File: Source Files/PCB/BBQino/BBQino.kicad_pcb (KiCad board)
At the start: 2 copper layers, 113 x 53.3 mm, 27 parts, among them J1 VIN < 13V, J2 230V input, J3 230V out, K1 FTR-MYAA005D, K2 FTR-MYAA005D, Q1 IPD068P03L3G, U1 ADP7142ARDZ-5.0, U99 24LC512

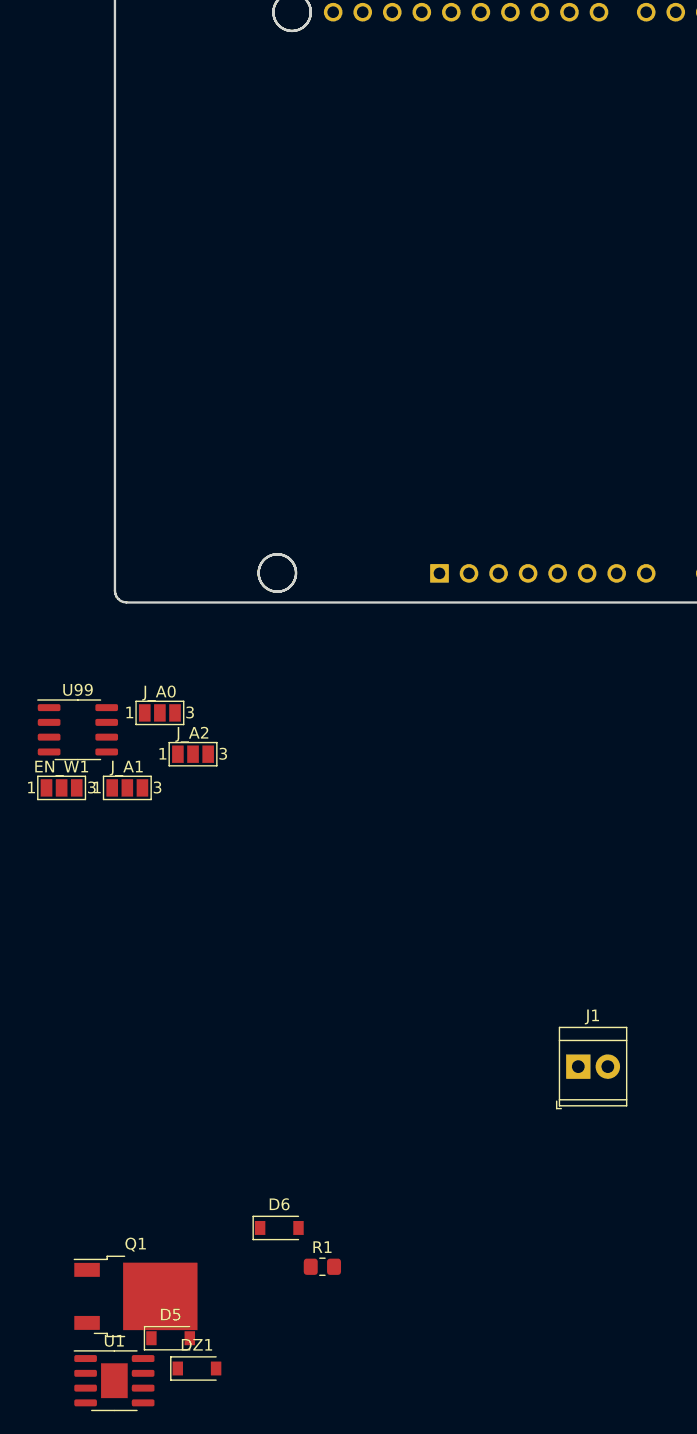
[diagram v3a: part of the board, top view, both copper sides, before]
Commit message: added thermocouple interface
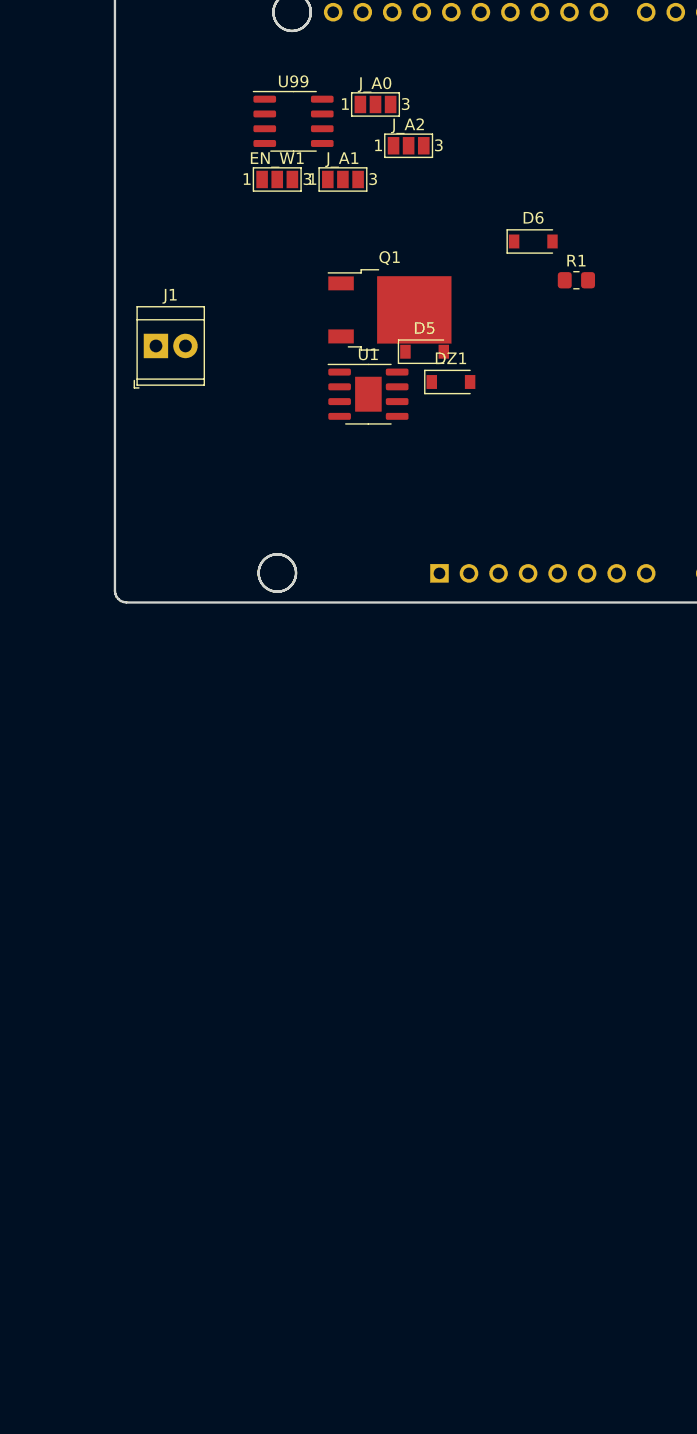
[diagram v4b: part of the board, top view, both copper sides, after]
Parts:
- moved D5 87.6 mm to (77.7, 60.9)
- moved DZ1 87.6 mm to (80.0, 63.6)
- moved R1 87.6 mm to (90.8, 54.8)
- moved D6 87.6 mm to (87.1, 51.5)
- moved Q1 87.6 mm to (74.7, 57.4)
- moved U1 87.6 mm to (72.9, 64.6)
- moved J1 71.8 mm to (54.6, 60.5)
- moved J_A0 55.5 mm to (73.5, 39.7)
- moved J_A2 55.5 mm to (76.3, 43.2)
- moved EN_W1 55.5 mm to (65.0, 46.1)
- moved J_A1 55.5 mm to (70.7, 46.1)
- moved U99 55.5 mm to (66.4, 41.1)
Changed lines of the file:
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@@
   )
   (module Diode_SMD:D_SOD-123 (layer F.Cu)
-    (at 65.221001 136.303001)
+    (at 87.065001 51.467001)
     (descr SOD-123)
     (tags SOD-123)
@@
   )
   (module Diode_SMD:D_SOD-123 (layer F.Cu)
-    (at 55.871001 145.783001)
+    (at 77.715001 60.947001)
     (descr SOD-123)
     (tags SOD-123)
@@
   )
   (module Package_SO:SOIC-8_3.9x4.9mm_P1.27mm (layer F.Cu)
-    (at 47.9 93.46)
+    (at 66.442 41.136)
     (descr "SOIC, 8 Pin (JEDEC MS-012AA, https://www.analog.com/media/en/package-pcb-resources/package/pkg_pdf/soic_narrow-r/r_8.pdf), generated with kicad-footprint-generator ipc_gullwing_generator.py")
     (tags "SOIC SO")
@@
   )
   (module Package_SO:SOIC-8-1EP_3.9x4.9mm_P1.27mm_EP2.29x3mm (layer F.Cu)
-    (at 51.036 149.438)
+    (at 72.88 64.602)
     (descr "SOIC, 8 Pin (https://www.analog.com/media/en/technical-documentation/data-sheets/ada4898-1_4898-2.pdf#page=29), generated with kicad-footprint-generator ipc_gullwing_generator.py")
     (tags "SOIC SO")
@@
   )
   (module Resistor_SMD:R_0805_2012Metric_Pad1.20x1.40mm_HandSolder (layer F.Cu)
-    (at 68.926 139.638)
+    (at 90.77 54.802)
     (descr "Resistor SMD 0805 (2012 Metric), square (rectangular) end terminal, IPC_7351 nominal with elongated pad for handsoldering. (Body size source: IPC-SM-782 page 72, https://www.pcb-3d.com/wordpress/wp-content/uploads/ipc-sm-782a_amendment_1_and_2.pdf), generated with kicad-footprint-generator")
     (tags "resistor handsolder")
@@
   )
   (module Package_TO_SOT_SMD:TO-252-2 (layer F.Cu)
-    (at 52.886 142.188)
+    (at 74.73 57.352)
     (descr "TO-252 / DPAK SMD package, http://www.infineon.com/cms/en/product/packages/PG-TO252/PG-TO252-3-1/")
     (tags "DPAK TO-252 DPAK-3 TO-252-3 SOT-428")
@@
   )
   (module Jumper:SolderJumper-3_P1.3mm_Open_Pad1.0x1.5mm_NumberLabels (layer F.Cu)
-    (at 57.8 95.56)
+    (at 76.342 43.236)
     (descr "SMD Solder Jumper, 1x1.5mm Pads, 0.3mm gap, open, labeled with numbers")
     (tags "solder jumper open")
@@
   )
   (module Jumper:SolderJumper-3_P1.3mm_Open_Pad1.0x1.5mm_NumberLabels (layer F.Cu)
-    (at 52.15 98.46)
+    (at 70.692 46.136)
     (descr "SMD Solder Jumper, 1x1.5mm Pads, 0.3mm gap, open, labeled with numbers")
     (tags "solder jumper open")
@@
   )
   (module Jumper:SolderJumper-3_P1.3mm_Open_Pad1.0x1.5mm_NumberLabels (layer F.Cu)
-    (at 54.95 92.01)
+    (at 73.492 39.686)
     (descr "SMD Solder Jumper, 1x1.5mm Pads, 0.3mm gap, open, labeled with numbers")
     (tags "solder jumper open")
@@
   )
   (module TerminalBlock_TE-Connectivity:TerminalBlock_TE_282834-2_1x02_P2.54mm_Horizontal (layer F.Cu)
-    (at 90.932 122.428)
+    (at 54.61 60.452)
     (descr "Terminal Block TE 282834-2, 2 pins, pitch 2.54mm, size 5.54x6.5mm^2, drill diamater 1.1mm, pad diameter 2.1mm, see http://www.te.com/commerce/DocumentDelivery/DDEController?Action=showdoc&DocId=Customer+Drawing%7F282834%7FC1%7Fpdf%7FEnglish%7FENG_CD_282834_C1.pdf, script-generated using https://github.com/pointhi/kicad-footprint-generator/scripts/TerminalBlock_TE-Connectivity")
     (tags "THT Terminal Block TE 282834-2 pitch 2.54mm size 5.54x6.5mm^2 drill 1.1mm pad 2.1mm")
@@
   )
   (module Jumper:SolderJumper-3_P1.3mm_Open_Pad1.0x1.5mm_NumberLabels (layer F.Cu)
-    (at 46.5 98.46)
+    (at 65.042 46.136)
     (descr "SMD Solder Jumper, 1x1.5mm Pads, 0.3mm gap, open, labeled with numbers")
     (tags "solder jumper open")
@@
   )
   (module Diode_SMD:D_SOD-123 (layer F.Cu)
-    (at 58.136 148.388)
+    (at 79.98 63.552)
     (descr SOD-123)
     (tags SOD-123)

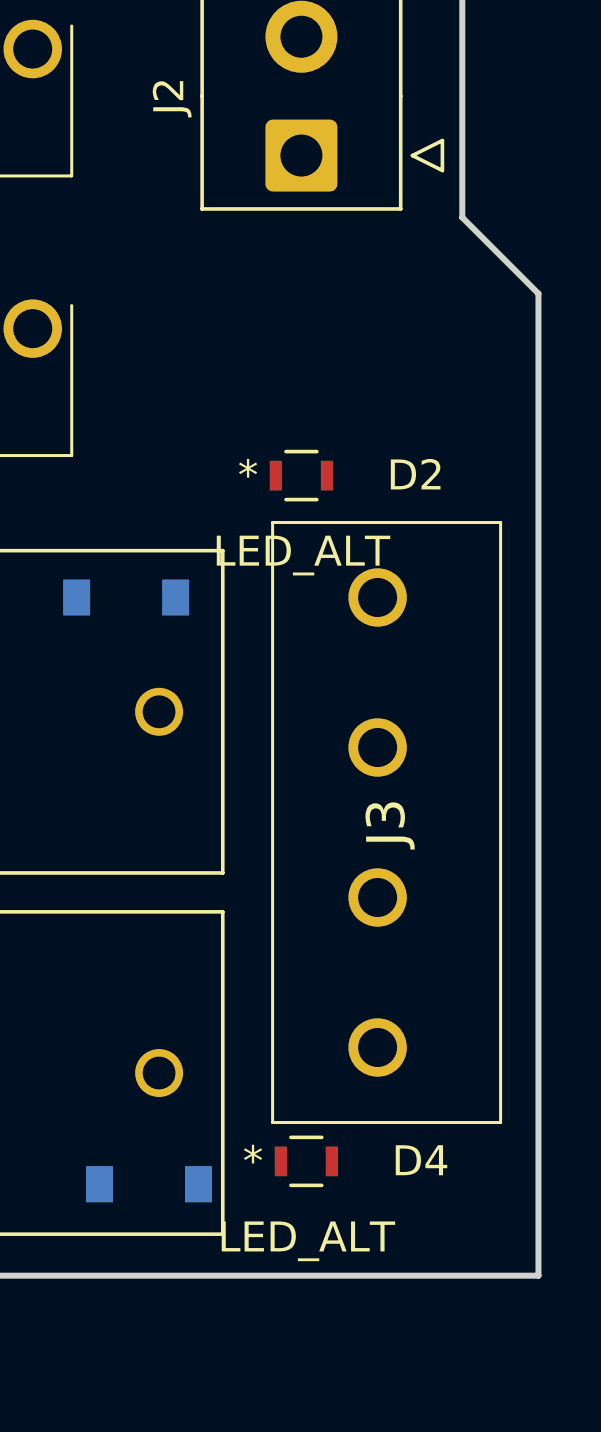
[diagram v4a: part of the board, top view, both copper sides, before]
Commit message: added current sense on motor side
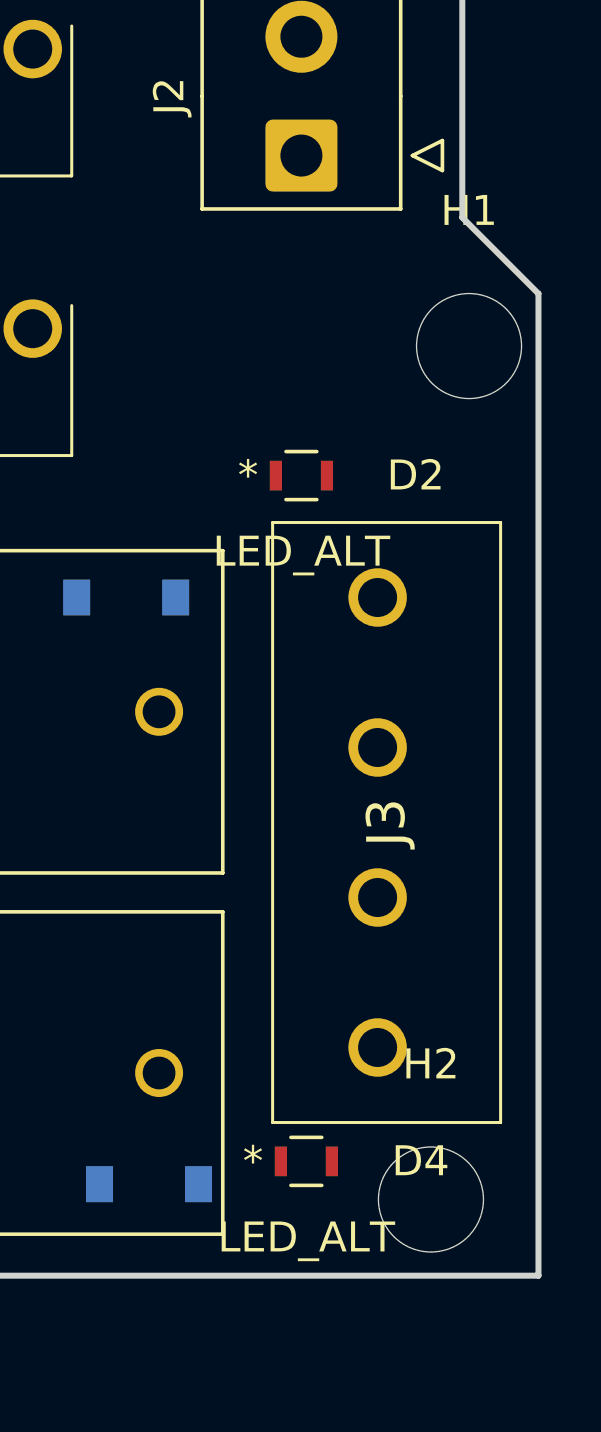
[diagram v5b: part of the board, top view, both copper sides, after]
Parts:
- added H1: MountingHole, MountingHole:MountingHole_3.5mm, F.Cu at (161.8, 46.2)
- added H2: MountingHole, MountingHole:MountingHole_3.5mm, F.Cu at (160.5, 74.7)

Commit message: updated schematic
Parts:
- added C2: 2.2uF, Capacitor_SMD:C_0805_2012Metric_Pad1.18x1.45mm_HandSolder, F.Cu at (55.9, 111.5)
- added C3: 10nF, Capacitor_SMD:C_0805_2012Metric_Pad1.18x1.45mm_HandSolder, F.Cu at (60.7, 111.5)
- added C4: 1nF, Capacitor_SMD:C_0805_2012Metric_Pad1.18x1.45mm_HandSolder, F.Cu at (80.2, 101.9)
- added C5: 2.2uF, Capacitor_SMD:C_0805_2012Metric_Pad1.18x1.45mm_HandSolder, F.Cu at (65.5, 111.5)
- added D7: 1N4148W-HF, Diode_SMD:D_SOD-123, F.Cu at (203.1, 66.8)
- added D8: 1N4148W-HF, Diode_SMD:D_SOD-123, F.Cu at (202.8, 61.6)
- added IC2: DG4052EEN-T1-GE4, BBQino:QFN40P180X260X60-16N-D, F.Cu at (104.2, 96.4)
- added IC3: MAX6675ISA+T, BBQino:SOIC127P600X175-8N, F.Cu at (97.9, 97.2)
- added K3: FINDER-40.41, Relay_THT:Relay_SPDT_Finder_40.41, F.Cu at (173.1, 51.6)
- added K4: FINDER-40.41, Relay_THT:Relay_SPDT_Finder_40.41, F.Cu at (173.1, 65.6)
- added Q2: DMP4051LK3, Package_TO_SOT_SMD:TO-252-3_TabPin2, F.Cu at (59.5, 97.9)
- added Q3: DMN4040SK3, Package_TO_SOT_SMD:TO-252-3_TabPin2, F.Cu at (59.5, 106.0)
- added Q4: DMP4051LK3, Package_TO_SOT_SMD:TO-252-3_TabPin2, F.Cu at (71.7, 97.9)
- added Q5: DMN4040SK3, Package_TO_SOT_SMD:TO-252-3_TabPin2, F.Cu at (71.7, 106.0)
- added Q6: 2N7002K, Package_TO_SOT_SMD:SOT-23, F.Cu at (203.1, 51.6)
- added Q7: 2N7002K, Package_TO_SOT_SMD:SOT-23, F.Cu at (207.6, 51.6)
- added R4: 330, Resistor_SMD:R_0805_2012Metric_Pad1.20x1.40mm_HandSolder, F.Cu at (70.3, 111.5)
- added R5: 330, Resistor_SMD:R_0805_2012Metric_Pad1.20x1.40mm_HandSolder, F.Cu at (80.2, 104.8)
- added U2: INA219AxD, Package_SO:SOIC-8_3.9x4.9mm_P1.27mm, F.Cu at (82.0, 97.1)
- added U3: INA181, Package_TO_SOT_SMD:SOT-23-6, F.Cu at (96.1, 106.4)
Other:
- board size 113 x 53.3 mm -> 158.5 x 53.3 mm

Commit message: New architecture
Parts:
- removed R4, R5: 330, Resistor_SMD:R_0805_2012Metric_Pad1.20x1.40mm_HandSolder
- removed U2: INA219AxD, Package_SO:SOIC-8_3.9x4.9mm_P1.27mm
- added C10: 1uF, Capacitor_SMD:C_0805_2012Metric_Pad1.18x1.45mm_HandSolder, F.Cu at (121.9, 10.6)
- added C11: 1uF, Capacitor_SMD:C_0805_2012Metric_Pad1.18x1.45mm_HandSolder, F.Cu at (113.9, 19.7)
- added C12: 1uF, Capacitor_SMD:C_0805_2012Metric_Pad1.18x1.45mm_HandSolder, F.Cu at (126.7, 7.62)
- added C19: 1uF, Capacitor_SMD:C_0805_2012Metric_Pad1.18x1.45mm_HandSolder, F.Cu at (118.7, 16.7)
- added C20: 1uF, Capacitor_SMD:C_0805_2012Metric_Pad1.18x1.45mm_HandSolder, F.Cu at (121.9, 13.6)
- added C21: 1uF, Capacitor_SMD:C_0805_2012Metric_Pad1.18x1.45mm_HandSolder, F.Cu at (126.7, 10.6)
- added C8: 2.2nF, Capacitor_SMD:C_0805_2012Metric_Pad1.18x1.45mm_HandSolder, F.Cu at (121.9, 7.62)
- added C9: 2.2nF, Capacitor_SMD:C_0805_2012Metric_Pad1.18x1.45mm_HandSolder, F.Cu at (113.9, 16.7)
- added D10: BAS316, Diode_SMD:D_SOD-323, F.Cu at (93.3, 49.1)
- added D11: BAS316, Diode_SMD:D_SOD-323, F.Cu at (74.6, 78.8)
- added D12: BAS316, Diode_SMD:D_SOD-323, F.Cu at (93.8, 45.4)
- added D13: BAS316, Diode_SMD:D_SOD-323, F.Cu at (89.1, 49.1)
- added D14: BAS316, Diode_SMD:D_SOD-323, F.Cu at (126.5, 13.6)
- added D15: BAS316, Diode_SMD:D_SOD-323, F.Cu at (118.4, 19.7)
- added D16: B140-E3, Diode_SMD:D_SMA, F.Cu at (115.5, 8.39)
- added D17: B140-E3, Diode_SMD:D_SMA, F.Cu at (115.5, 12.9)
- added D18: BZM55Bxx, Diode_SMD:D_MicroMELF, F.Cu at (131.8, 16.6)
- added D19: BZM55Bxx, Diode_SMD:D_MicroMELF, F.Cu at (131.8, 19.3)
- added D9: SD36_SOD323, Diode_SMD:D_SOD-323, F.Cu at (101.8, 36.5)
- added J4: 230V_1_presence, TerminalBlock_Phoenix:TerminalBlock_Phoenix_PT-1,5-2-3.5-H_1x02_P3.50mm_Horizontal, F.Cu at (134.6, 38.1)
- added J5: Screw_Terminal_01x02-Connector, TerminalBlock_Phoenix:TerminalBlock_Phoenix_PT-1,5-2-3.5-H_1x02_P3.50mm_Horizontal, F.Cu at (55.9, 61.0)
- added J6: 230v_2_presence, TerminalBlock_Phoenix:TerminalBlock_Phoenix_PT-1,5-2-3.5-H_1x02_P3.50mm_Horizontal, F.Cu at (142.2, 38.1)
- added Q10: IPD025N06N, Package_TO_SOT_SMD:TO-252-3_TabPin2, F.Cu at (101.5, 58.1)
- added Q11: IPD025N06N, Package_TO_SOT_SMD:TO-252-3_TabPin2, F.Cu at (101.5, 66.2)
- added Q12: BC846BPN, Package_TO_SOT_SMD:SOT-363_SC-70-6, F.Cu at (127.7, 17.1)
- added Q13: BC846BPN, Package_TO_SOT_SMD:SOT-363_SC-70-6, F.Cu at (135.7, 12.6)
- added Q8: IPD025N06N, Package_TO_SOT_SMD:TO-252-3_TabPin2, F.Cu at (89.4, 58.1)
- added Q9: IPD025N06N, Package_TO_SOT_SMD:TO-252-3_TabPin2, F.Cu at (89.4, 66.2)
- added R18: 10, Resistor_SMD:R_0805_2012Metric_Pad1.20x1.40mm_HandSolder, F.Cu at (90.4, 71.7)
- added R19: 10, Resistor_SMD:R_0805_2012Metric_Pad1.20x1.40mm_HandSolder, F.Cu at (93.6, 42.4)
- added R20: 10k, Resistor_SMD:R_0805_2012Metric_Pad1.20x1.40mm_HandSolder, F.Cu at (95.2, 71.7)
- added R21: 10k, Resistor_SMD:R_0805_2012Metric_Pad1.20x1.40mm_HandSolder, F.Cu at (99.9, 71.7)
- added R22: 3.3, Resistor_SMD:R_0805_2012Metric_Pad1.20x1.40mm_HandSolder, F.Cu at (70.6, 72.9)
- added R23: 20m, Resistor_SMD:R_0805_2012Metric_Pad1.20x1.40mm_HandSolder, F.Cu at (93.6, 36.5)
- added R24: 1k, Resistor_SMD:R_0805_2012Metric_Pad1.20x1.40mm_HandSolder, F.Cu at (104.7, 71.7)
- added R25: 3.3, Resistor_SMD:R_0805_2012Metric_Pad1.20x1.40mm_HandSolder, F.Cu at (70.6, 75.8)
- added R26: 10k, Resistor_SMD:R_0805_2012Metric_Pad1.20x1.40mm_HandSolder, F.Cu at (93.6, 39.5)
- added R27: 10k, Resistor_SMD:R_0805_2012Metric_Pad1.20x1.40mm_HandSolder, F.Cu at (89.3, 46.2)
- added R28: 10, Resistor_SMD:R_0805_2012Metric_Pad1.20x1.40mm_HandSolder, F.Cu at (70.1, 79.3)
- added R29: 10, Resistor_SMD:R_0805_2012Metric_Pad1.20x1.40mm_HandSolder, F.Cu at (85.7, 71.7)
- added R34: 1k, Resistor_SMD:R_0805_2012Metric_Pad1.20x1.40mm_HandSolder, F.Cu at (80.0, 35.6)
- added R35: 10k, Resistor_SMD:R_0805_2012Metric_Pad1.20x1.40mm_HandSolder, F.Cu at (80.0, 38.5)
- added R36: 10k, Resistor_SMD:R_0805_2012Metric_Pad1.20x1.40mm_HandSolder, F.Cu at (84.8, 35.6)
- added R37: 10k, Resistor_SMD:R_0805_2012Metric_Pad1.20x1.40mm_HandSolder, F.Cu at (84.8, 38.5)
- added R38: 10k, Resistor_SMD:R_0805_2012Metric_Pad1.20x1.40mm_HandSolder, F.Cu at (89.5, 35.6)
- Q2, Q4: value DMP4051LK3 -> BC846; footprint Package_TO_SOT_SMD:TO-252-3_TabPin2 -> Package_TO_SOT_SMD:SOT-23
- Q3, Q5: value DMN4040SK3 -> BC846; footprint Package_TO_SOT_SMD:TO-252-3_TabPin2 -> Package_TO_SOT_SMD:SOT-23
- moved Q5 116.8 mm to (135.8, 8.39)
- moved Q2 114.8 mm to (131.4, 8.39)
- moved Q3 109.1 mm to (123.3, 17.4)
- moved Q4 103.8 mm to (131.4, 12.9)
- moved U3 54.6 mm to (97.4, 51.8)
- moved IC2 54.6 mm to (105.5, 41.7)
- moved IC3 54.6 mm to (99.2, 42.6)
- moved C2 48.6 mm to (87.6, 74.7)
- moved C3 48.6 mm to (92.4, 74.7)
- moved C4 48.6 mm to (111.9, 65.0)
- moved C5 48.6 mm to (97.2, 74.7)
- moved R1 10.1 mm to (86.4, 45.7)
- moved K1 5.96 mm to (129.5, 45.7)
- moved J1 4.57 mm to (54.6, 55.9), turned to 90 degrees
- moved DZ1 2.84 mm to (78.7, 66.1)
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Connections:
- net GNDPWR renamed I_MOTOR_N
- Q2 pad 1: Net-(IC1-Pad8) -> Net-(Q2-Pad1)
- Q2 pad 2: Net-(C8-Pad2) -> GNDD
- Q2 pad 3: +12V -> Net-(Q2-Pad3)
- Q3 pad 1: Net-(IC1-Pad8) -> Net-(Q3-Pad1)
- Q3 pad 2: Net-(C8-Pad2) -> GNDD
- Q4 pad 1: Net-(IC1-Pad6) -> Net-(D18-Pad1)
- Q4 pad 2: Net-(C11-Pad2) -> Net-(C20-Pad1)
- Q4 pad 3: +12V -> Net-(C10-Pad1)
- Q5 pad 1: Net-(IC1-Pad6) -> Net-(D19-Pad1)
- Q5 pad 2: Net-(C11-Pad2) -> Net-(C21-Pad1)
- Q5 pad 3: Net-(Q3-Pad3) -> Net-(C11-Pad1)
